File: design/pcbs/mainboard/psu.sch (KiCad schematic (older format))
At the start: 67 parts, among them K1 EC2-5NU, K2 EC2-5NU, U19 TPS7A49, U20 TPS7A30, U3 TLV1117-33, U4 TPS7A49, U5 TPS7A30

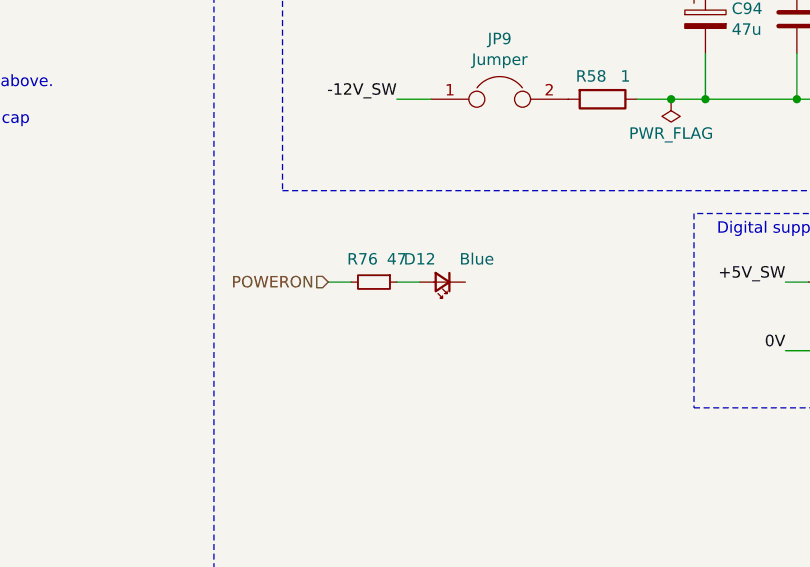
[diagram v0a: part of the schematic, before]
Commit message: Completed layout of main board, cleaned up some libraries.
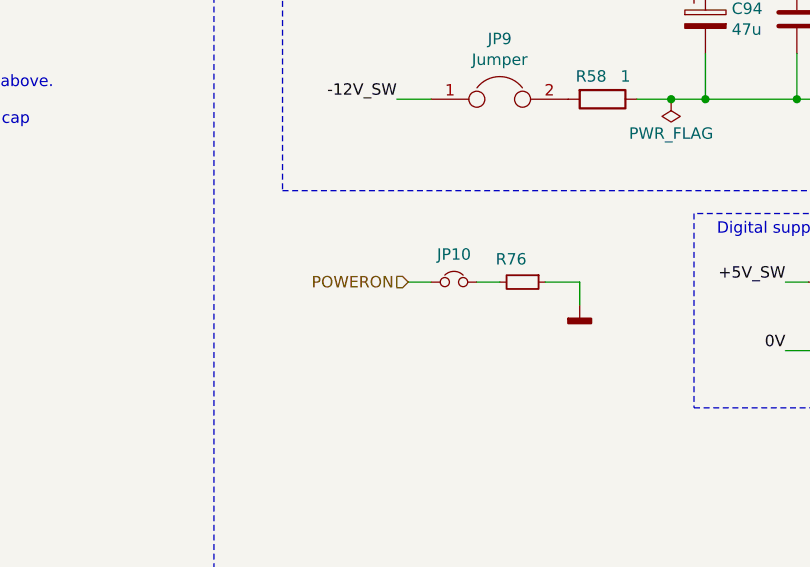
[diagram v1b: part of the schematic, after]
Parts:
- removed D12: Blue, LED_SMD:LED_0603_1608Metric, symbol Device:LED_Small
- added JP10: ~, Connector_PinHeader_2.54mm:PinHeader_1x02_P2.54mm_Vertical, symbol Device:Jumper_NC_Small
- R76: value 47 -> ~; footprint Resistor_SMD:R_0402_1005Metric -> Resistor_THT:R_Axial_DIN0204_L3.6mm_D1.6mm_P5.08mm_Horizontal; Done Yes -> (none); LCSC C25118 -> (none)
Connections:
- net GNDD: now also R76.1
- net POWERON: now also JP10.1; no longer R76.2
- new net: JP10.2, R76.2
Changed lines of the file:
@@
+	1    0    0    -1
+$EndComp
+Wire Wire Line
+	6750 5950 6650 5950
+Wire Wire Line
+	6450 5950 6350 5950
+Text HLabel 6350 5950 0    50   Input ~ 0
+POWERON
+$Comp
+L Device:Jumper_NC_Small JP?
+U 1 1 5EF82B26
+P 6550 5950
+AR Path="/5EC75F5F/5EF82B26" Ref="JP?"  Part="1"
+AR Path="/5EC7824B/5EF82B26" Ref="JP10"  Part="1"
+F 0 "JP10" H 6550 6071 50  0000 C CNN
+F 1 "~" H 6550 6071 50  0000 C CNN
+F 2 "Connector_PinHeader_2.54mm:PinHeader_1x02_P2.54mm_Vertical" H 6550 5950 50  0001 C CNN
+F 3 "~" H 6550 5950 50  0001 C CNN
+F 4 "Yes" H 6550 5950 50  0001 C CNN "Done"
+	1    6550 5950
 	1    0    0    -1
 $EndComp
 $Comp
-L Device:LED_Small D?
-U 1 1 5EF22E48
-P 6500 5950
-AR Path="/5EC75F5F/5EF22E48" Ref="D?"  Part="1"
-AR Path="/5EC7824B/5EF22E48" Ref="D12"  Part="1"
-F 0 "D12" H 6600 5850 50  0000 C CNN
-F 1 "Blue" H 6350 5850 50  0000 C CNN
-F 2 "LED_SMD:LED_0603_1608Metric" V 6500 5950 50  0001 C CNN
-F 3 "https://datasheet.lcsc.com/szlcsc/Everlight-Elec-19-217-BHC-ZL1M2RY-3T_C72041.pdf" V 6500 5950 50  0001 C CNN
-F 4 "C72041" H 6500 5950 50  0001 C CNN "LCSC"
-F 5 "Yes" H 6500 5950 50  0001 C CNN "Done"
-	1    6500 5950
-	-1   0    0    1
+L Device:R_Small R?
+U 1 1 5EF82B2F
+P 6850 5950
+AR Path="/5EC75F5F/5EF82B2F" Ref="R?"  Part="1"
+AR Path="/5EC7824B/5EF82B2F" Ref="R76"  Part="1"
+F 0 "R76" V 6750 5900 50  0000 C CNN
+F 1 "~" V 6750 6050 50  0000 C CNN
+F 2 "Resistor_THT:R_Axial_DIN0204_L3.6mm_D1.6mm_P5.08mm_Horizontal" V 6780 5950 50  0001 C CNN
+F 3 "" H 6850 5950 50  0001 C CNN
+F 4 "" V 6850 5950 50  0001 C CNN "LCSC"
+F 5 "" V 6850 5950 50  0001 C CNN "Done"
+	1    6850 5950
+	0    1    1    0
 $EndComp
 $Comp
-L Device:R_Small R?
-U 1 1 5EF22E56
-P 6200 5950
-AR Path="/5EC75F5F/5EF22E56" Ref="R?"  Part="1"
-AR Path="/5EC7824B/5EF22E56" Ref="R76"  Part="1"
-F 0 "R76" V 6100 5900 50  0000 C CNN
-F 1 "47" V 6100 6050 50  0000 C CNN
-F 2 "Resistor_SMD:R_0402_1005Metric" V 6130 5950 50  0001 C CNN
-F 3 "https://datasheet.lcsc.com/szlcsc/Uniroyal-Elec-0402WGF470JTCE_C25118.pdf" H 6200 5950 50  0001 C CNN
-F 4 "C25118" V 6200 5950 50  0001 C CNN "LCSC"
-F 5 "Yes" V 6200 5950 50  0001 C CNN "Done"
-	1    6200 5950
-	0    1    1    0
+L power:GNDD #PWR031
+U 1 1 5EF9691F
+P 7100 6050
+F 0 "#PWR031" H 7100 5800 50  0001 C CNN
+F 1 "GNDD" H 7104 5895 50  0001 C CNN
+F 2 "" H 7100 6050 50  0001 C CNN
+F 3 "" H 7100 6050 50  0001 C CNN
+	1    7100 6050
+	1    0    0    -1
 $EndComp
-Text HLabel 6000 5950 0    50   Input ~ 0
-POWERON
 Wire Wire Line
-	6100 5950 6000 5950
+	7100 6050 7100 5950
 Wire Wire Line
-	6400 5950 6300 5950
+	7100 5950 6950 5950
 $EndSCHEMATC

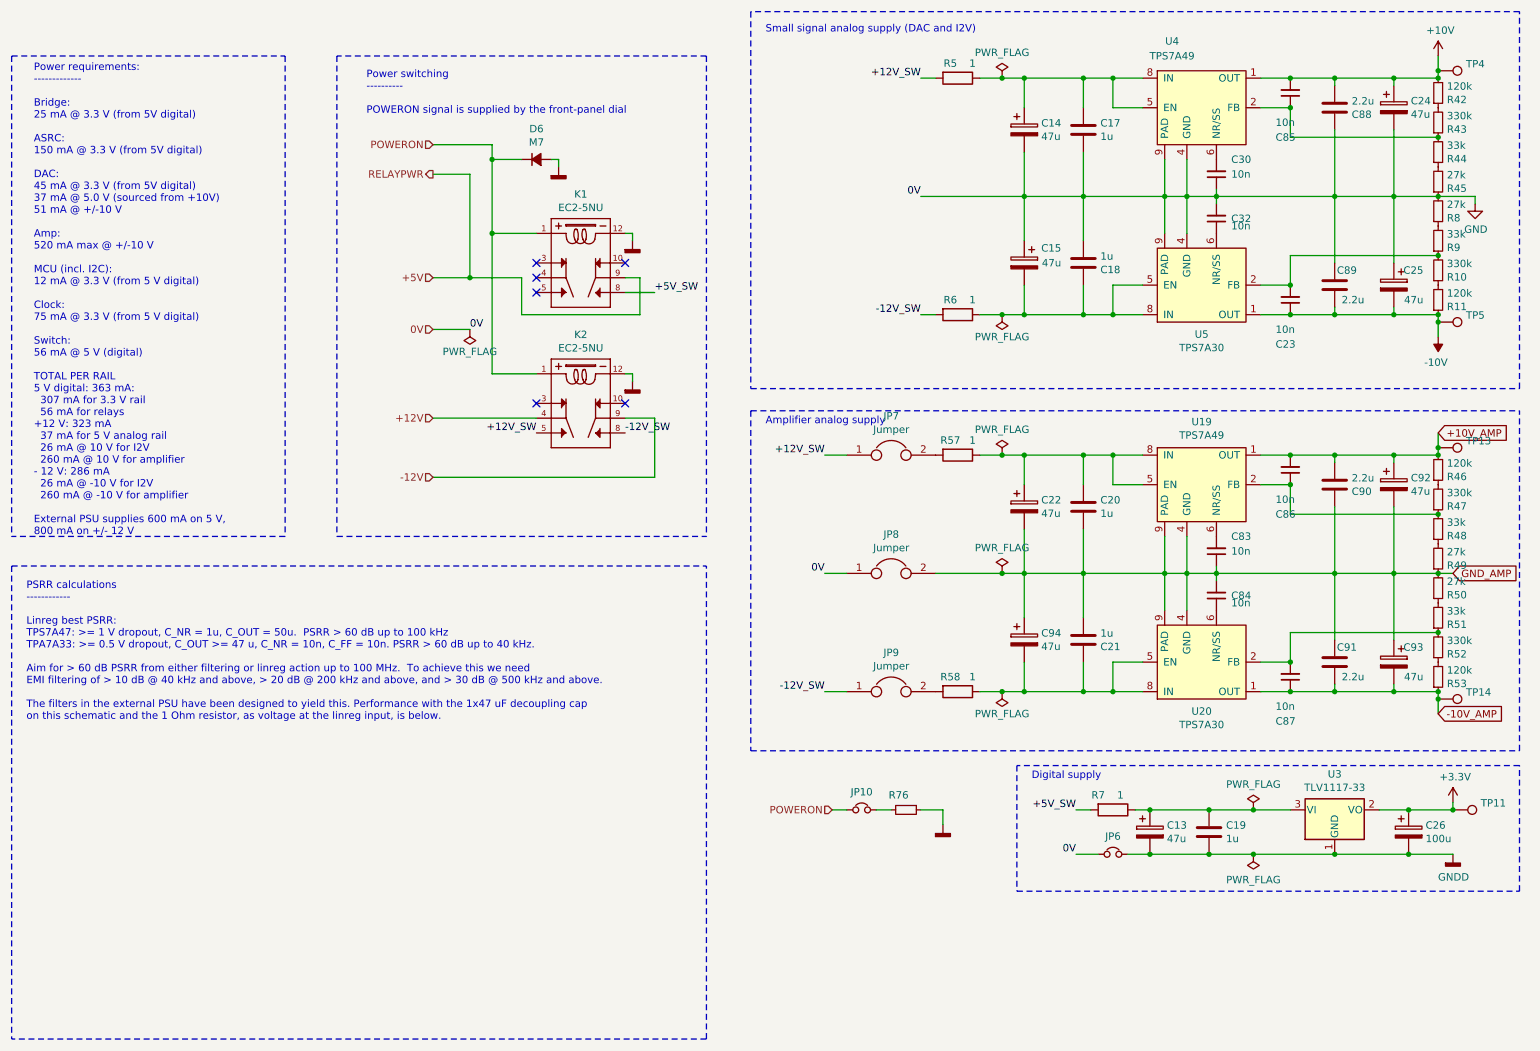
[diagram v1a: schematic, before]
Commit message: Renumbered footprints to follow board position.
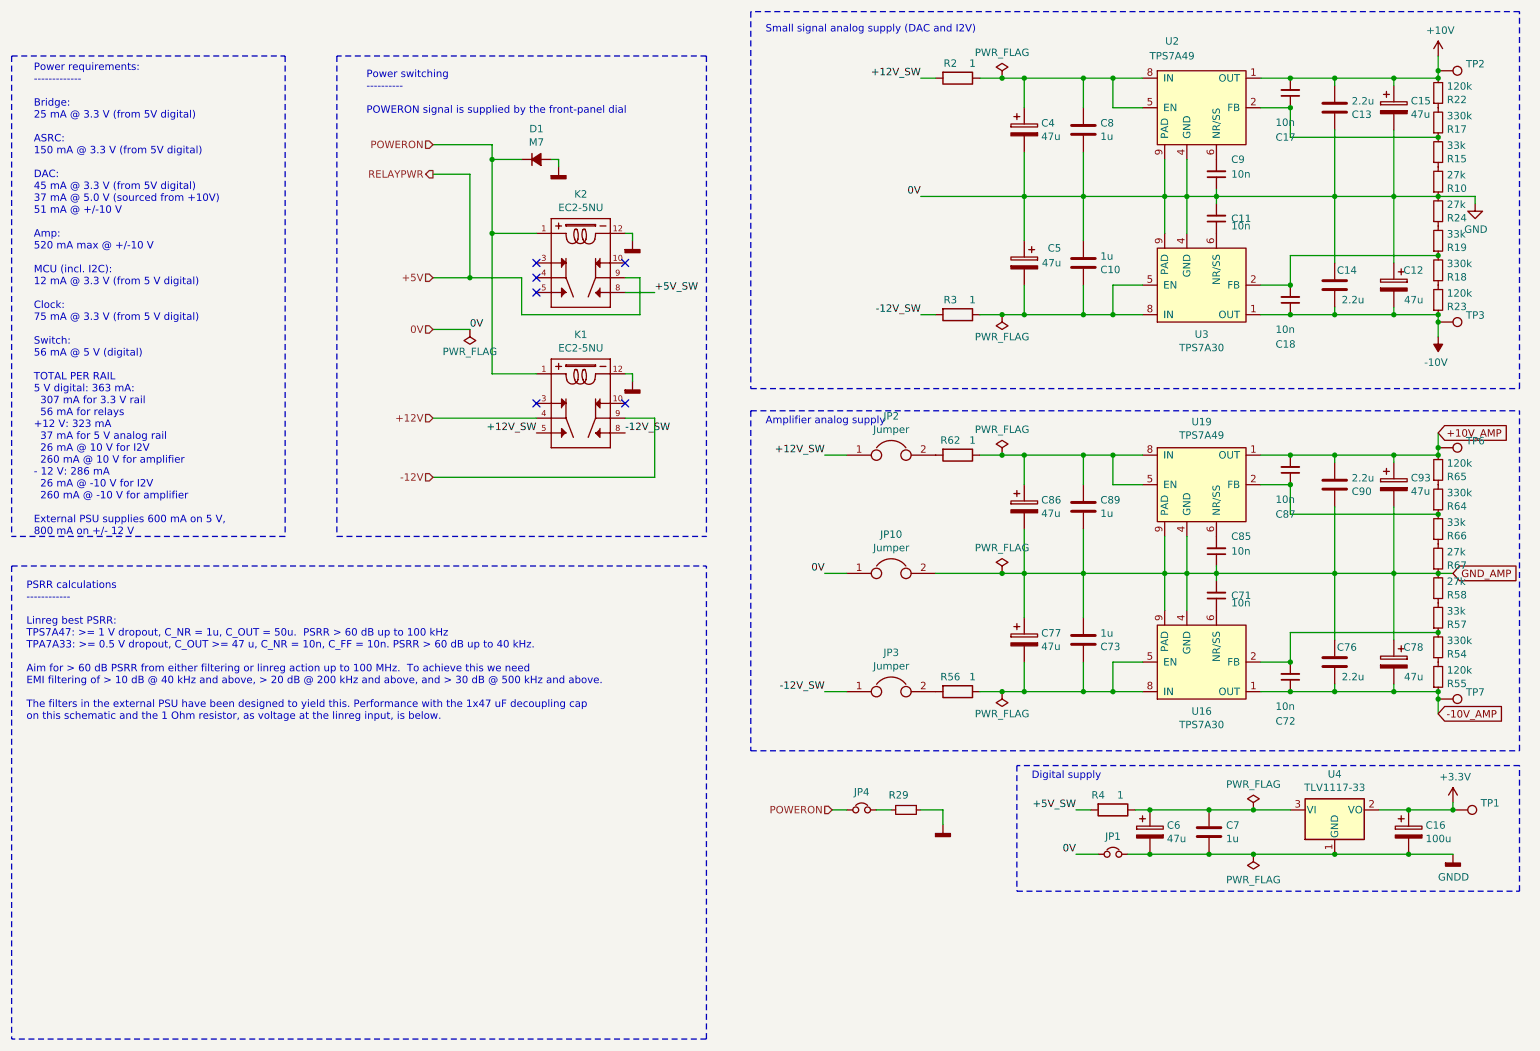
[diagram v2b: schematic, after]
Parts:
- renumbered C18 to C10, C32 to C11, C25 to C12, C88 to C13, C89 to C14, C24 to C15, C26 to C16, C85 to C17, C23 to C18, C14 to C4, C15 to C5, C13 to C6, C19 to C7, C84 to C71, C87 to C72, C21 to C73, C91 to C76, C94 to C77, C93 to C78, C17 to C8, C83 to C85, C22 to C86, C86 to C87, C20 to C89, C30 to C9, C92 to C93, D6 to D1, JP6 to JP1, JP8 to JP10, JP7 to JP2, JP9 to JP3, JP10 to JP4, K2 to K1, K1 to K2, R45 to R10, R44 to R15, R43 to R17, R10 to R18, R9 to R19, R5 to R2, R42 to R22, R11 to R23, R8 to R24, R76 to R29, R6 to R3, R7 to R4, R52 to R54, R53 to R55, R58 to R56, R51 to R57, R50 to R58, R57 to R62, R47 to R64, R46 to R65, R48 to R66, R49 to R67, TP11 to TP1, TP4 to TP2, TP5 to TP3, TP13 to TP6, TP14 to TP7, U20 to U16, U4 to U2, U5 to U3, U3 to U4

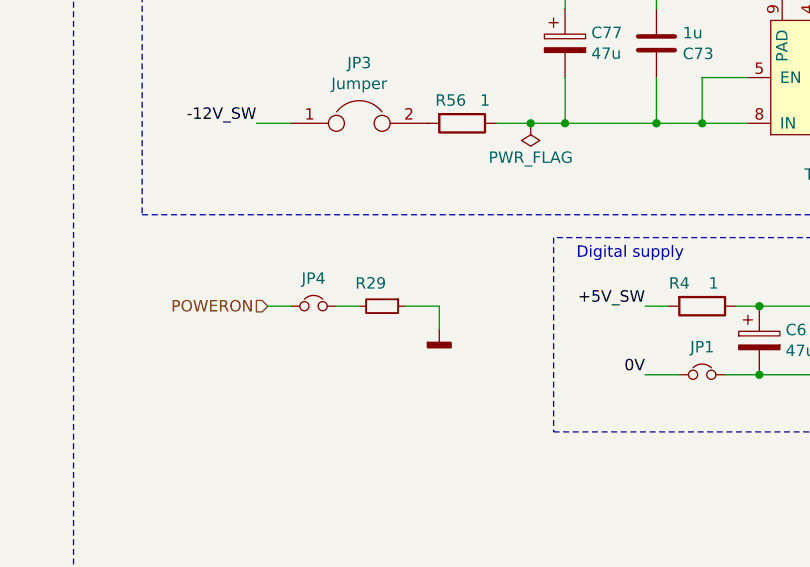
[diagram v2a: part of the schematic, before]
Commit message: Updated PCB sheet info. Clarified licence in readme.
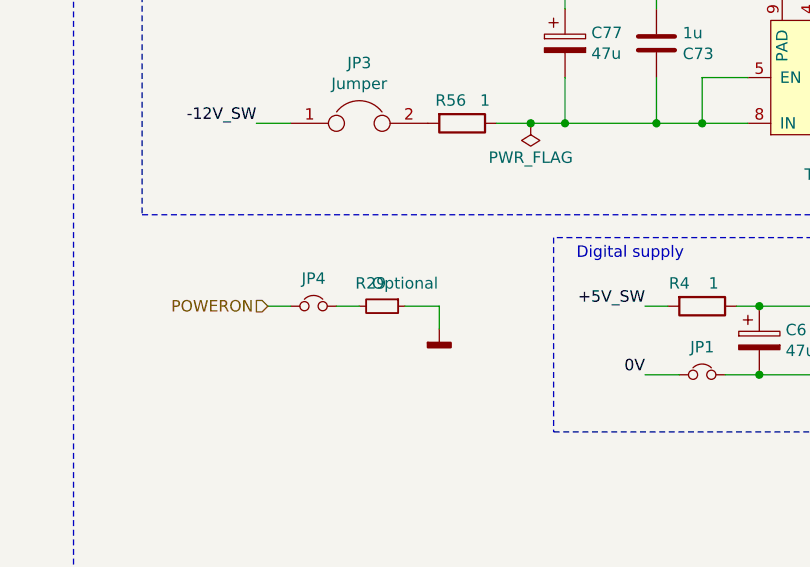
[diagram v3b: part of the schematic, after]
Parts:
- R29: value ~ -> Optional
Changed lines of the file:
@@
 AR Path="/5EC7824B/5EF82B2F" Ref="R29"  Part="1"
 F 0 "R29" V 6750 5900 50  0000 C CNN
-F 1 "~" V 6750 6050 50  0000 C CNN
+F 1 "Optional" V 6750 6050 50  0000 C CNN
 F 2 "Resistor_THT:R_Axial_DIN0204_L3.6mm_D1.6mm_P5.08mm_Horizontal" V 6780 5950 50  0001 C CNN
 F 3 "" H 6850 5950 50  0001 C CNN

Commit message: Fixed title blocks. Added fab outputs.
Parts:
- U16, U3: LCSC (none) -> C33835
- U19, U2: LCSC (none) -> C16430
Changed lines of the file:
@@
 encoding utf-8
 Sheet 3 10
-Title ""
-Date ""
-Rev ""
-Comp ""
-Comment1 ""
-Comment2 ""
+Title "DAC1 Main board"
+Date "2020-06-27"
+Rev "1.0.0"
+Comp "© Mark Pinese 2020"
+Comment1 "To view a copy of this license, visit https://creativecommons.org/licenses/by/4.0"
+Comment2 "This work is licensed under CC BY 4.0."
 Comment3 ""
 Comment4 ""
@@
 F 4 "296-27751-1-ND" H 8850 1200 50  0001 C CNN "DigiKey"
 F 5 "Yes" H 8850 1200 50  0001 C CNN "Done"
+F 6 "C16430" H 8850 1200 50  0001 C CNN "LCSC"
 	1    8850 1200
 	1    0    0    -1
@@
 F 4 "296-27750-1-ND" H 8850 2400 50  0001 C CNN "DigiKey"
 F 5 "Yes" H 8850 2400 50  0001 C CNN "Done"
+F 6 "C33835" H 8850 2400 50  0001 C CNN "LCSC"
 	1    8850 2400
 	1    0    0    1
@@
 F 4 "296-27751-1-ND" H 8850 3750 50  0001 C CNN "DigiKey"
 F 5 "Yes" H 8850 3750 50  0001 C CNN "Done"
+F 6 "C16430" H 8850 3750 50  0001 C CNN "LCSC"
 	1    8850 3750
 	1    0    0    -1
@@
 F 4 "296-27750-1-ND" H 8850 4950 50  0001 C CNN "DigiKey"
 F 5 "Yes" H 8850 4950 50  0001 C CNN "Done"
+F 6 "C33835" H 8850 4950 50  0001 C CNN "LCSC"
 	1    8850 4950
 	1    0    0    1
